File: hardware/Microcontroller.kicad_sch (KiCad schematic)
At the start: 10 parts

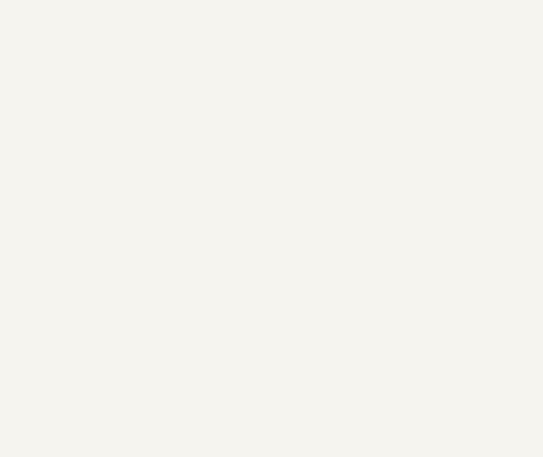
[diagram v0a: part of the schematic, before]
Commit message: added testpoints
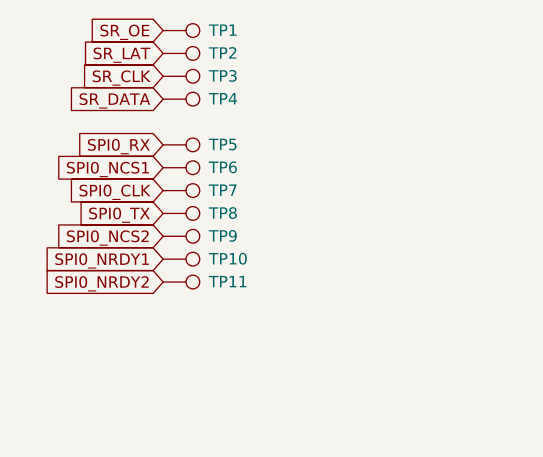
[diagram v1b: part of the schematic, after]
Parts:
- added TP1, TP10, TP11, TP2, TP3, TP4, TP5, TP6, TP7, TP8, TP9: TestPoint, TestPoint:TestPoint_THTPad_D1.5mm_Drill0.7mm, symbol Connector:TestPoint
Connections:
- net SPI0_CLK: now also TP7.1
- net SPI0_NCS1: now also TP6.1
- net SPI0_NCS2: now also TP9.1
- net SPI0_NRDY1: now also TP10.1
- net SPI0_NRDY2: now also TP11.1
- net SPI0_RX: now also TP5.1
- net SPI0_TX: now also TP8.1
- net SR_CLK: now also TP3.1
- net SR_DATA: now also TP4.1
- net SR_LAT: now also TP2.1
- net SR_OE: now also TP1.1

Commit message: final board, pinouts unchecked
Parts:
- TP1, TP10, TP11, TP2, TP3, TP4, TP5, TP6, TP7, TP8, TP9: Part Source Uni -> -
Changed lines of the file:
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@@
 			)
 		)
-		(property "Part Source" "Uni"
+		(property "Part Source" "-"
 			(at 38.1 63.5 90)
 			(hide yes)
@@
 			)
 		)
-		(property "Part Source" "Uni"
+		(property "Part Source" "-"
 			(at 38.1 55.88 90)
 			(hide yes)
@@
 			)
 		)
-		(property "Part Source" "Uni"
+		(property "Part Source" "-"
 			(at 38.1 43.18 90)
 			(hide yes)
@@
 			)
 		)
-		(property "Part Source" "Uni"
+		(property "Part Source" "-"
 			(at 38.1 66.04 90)
 			(hide yes)
@@
 			)
 		)
-		(property "Part Source" "Uni"
+		(property "Part Source" "-"
 			(at 38.1 53.34 90)
 			(hide yes)
@@
 			)
 		)
-		(property "Part Source" "Uni"
+		(property "Part Source" "-"
 			(at 38.1 40.64 90)
 			(hide yes)
@@
 			)
 		)
-		(property "Part Source" "Uni"
+		(property "Part Source" "-"
 			(at 38.1 45.72 90)
 			(hide yes)
@@
 			)
 		)
-		(property "Part Source" "Uni"
+		(property "Part Source" "-"
 			(at 38.1 50.8 90)
 			(hide yes)
@@
 			)
 		)
-		(property "Part Source" "Uni"
+		(property "Part Source" "-"
 			(at 38.1 58.42 90)
 			(hide yes)
@@
 			)
 		)
-		(property "Part Source" "Uni"
+		(property "Part Source" "-"
 			(at 38.1 38.1 90)
 			(hide yes)
@@
 			)
 		)
-		(property "Part Source" "Uni"
+		(property "Part Source" "-"
 			(at 38.1 60.96 90)
 			(hide yes)

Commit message: added signed declaration and updated schematic names
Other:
- company: (none) -> Amon Benson, TU Berlin
- title: (none) -> Microcontroller
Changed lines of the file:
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@@
 	(generator_version "10.0")
 	(paper "A4")
+	(title_block
+		(title "Microcontroller")
+		(date "2026-09-27")
+		(rev "1.0")
+		(company "Amon Benson, TU Berlin")
+	)
 	(junction
 		(at 110.49 119.38)
